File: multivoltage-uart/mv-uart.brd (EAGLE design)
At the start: 37.9 x 33.5 mm, 39 parts, among them SW1 DIP_SP6T, U1 IP4234CZ6, U2 CP2105-GM, U3 LDO_SHD_ADJ-AP2127K-ADJ, X1 MINI-USB-SHIELD-UX60-MB-5ST

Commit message: mv-uart: Add digikey link for all major parts
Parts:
- R1: value 18k -> 18k 1%

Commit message: Complete BOM attributes + export BOM
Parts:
- C3: value 2.2u -> 4.7u

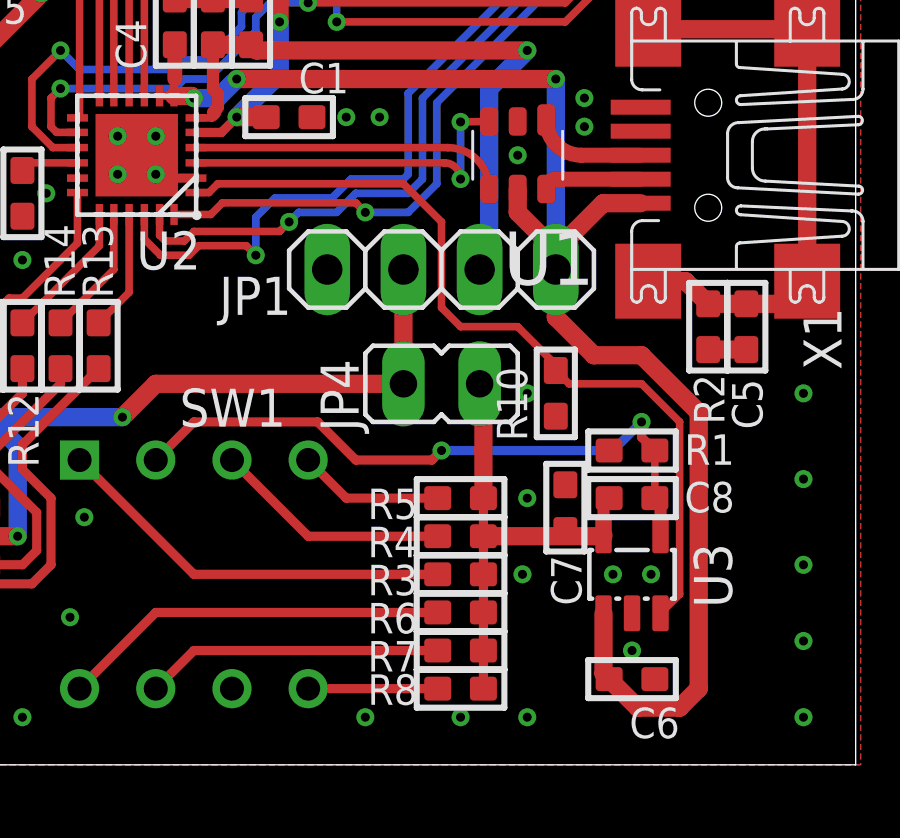
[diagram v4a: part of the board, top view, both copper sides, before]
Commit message: mv-uart: Fix 'board doesn't enumerate if JP4 is closed" issue
Make sure the LDO is always powered up, so the CP2105 internal and
external !RESET pull-ups are towards an active VIO voltage, rather than
one that is switched off by !SUSPEND and thus keeps the CP2105 in reset.

Closes: #1870 (https://osmocom.org/issues/1870)
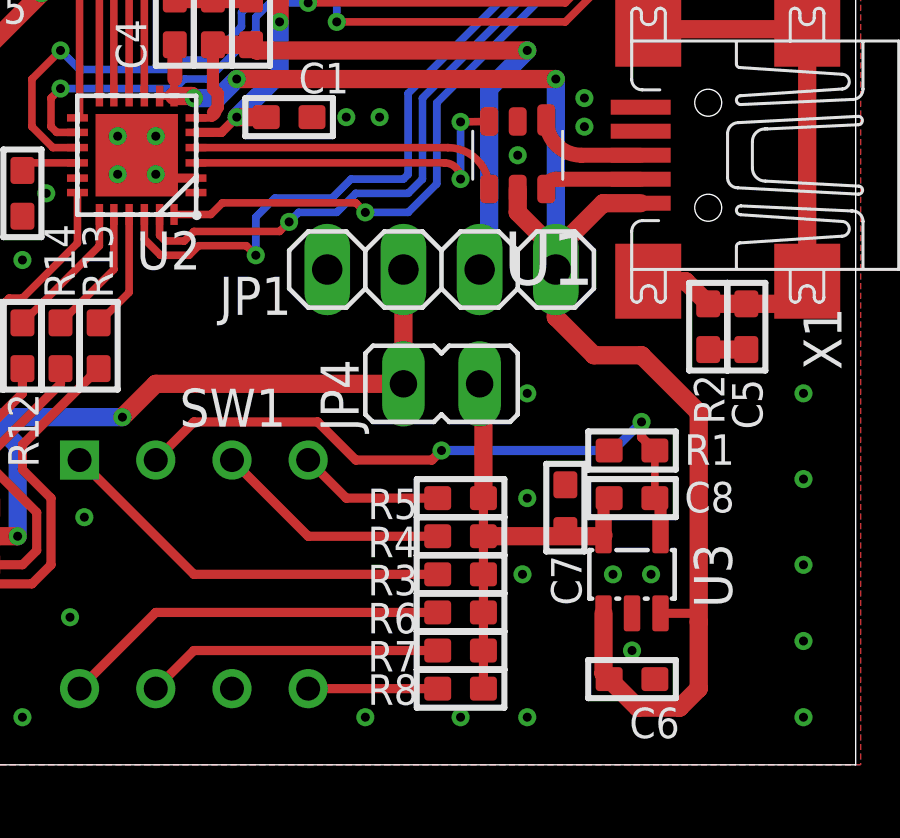
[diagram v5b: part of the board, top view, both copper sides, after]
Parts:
- removed R10: 10k, rc-sysmocom:_0603
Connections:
- net !SUSPEND: no longer R10.2, U3.3
- net GND: no longer R10.1
- net USB_VBUS: now also U3.3
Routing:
- net !SUSPEND: track 28.0 -> 0.00 mm
- net USB_VBUS: track 51.0 -> 52.6 mm
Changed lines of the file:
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@@
 </plain>
 <attributes>
-<attribute name="VERSION" value="v1"/>
+<attribute name="VERSION" value="v2"/>
 </attributes>
 <variantdefs>
@@
 <param name="TopRouterVariant" value="1"/>
 <param name="tpViaShape" value="round"/>
-<param name="PrefDir.1" value="a"/>
+<param name="PrefDir.1" value="|"/>
 <param name="PrefDir.2" value="0"/>
 <param name="PrefDir.3" value="0"/>
@@
 <param name="PrefDir.14" value="0"/>
 <param name="PrefDir.15" value="0"/>
-<param name="PrefDir.16" value="a"/>
+<param name="PrefDir.16" value="-"/>
 <param name="cfVia" value="8"/>
 <param name="cfNonPref" value="5"/>
@@
 <attribute name="LINK" value="http://www.digikey.com/product-detail/en/yageo/RC0603FR-0718KL/311-18.0KHRCT-ND/729936" x="30.48" y="10.4775" size="1.778" layer="27" display="off"/>
 </element>
-<element name="R10" library="rc-sysmocom" package="_0603" value="10k" x="27.94" y="12.3825" smashed="yes" rot="R90">
-<attribute name="NAME" x="26.9875" y="10.795" size="1.016" layer="25" font="vector" ratio="14" rot="R90"/>
-<attribute name="VALUE" x="29.4323" y="10.795" size="0.508" layer="27" font="vector" ratio="10" rot="R90"/>
-<attribute name="DESCRIPTION" value="RES SMD 10K OHM 5% 1/10W 0603" x="27.94" y="12.3825" size="1.778" layer="27" rot="R90" display="off"/>
-<attribute name="MANUFACTURER" value="Samsung Electro-Mechanics America, Inc." x="27.94" y="12.3825" size="1.778" layer="27" rot="R90" display="off"/>
-<attribute name="MANUFACTURERPARTNUMBER" value="RC1608J103CS" x="27.94" y="12.3825" size="1.778" layer="27" rot="R90" display="off"/>
-<attribute name="SOURCE" value="DIGIKEY" x="27.94" y="12.3825" size="1.778" layer="27" rot="R90" display="off"/>
-<attribute name="SOURCEPARTNUMBER" value="1276-5086-1-ND" x="27.94" y="12.3825" size="1.778" layer="27" rot="R90" display="off"/>
-<attribute name="ROHSCERTIFICATE" value="UNKNOWN ROHS CERTIFICATE" x="27.94" y="12.3825" size="1.778" layer="27" rot="R90" display="off"/>
-<attribute name="POPULATED" value="TRUE" x="27.94" y="12.3825" size="1.778" layer="27" rot="R90" display="off"/>
-<attribute name="CLASS" value="RESISTOR" x="27.94" y="12.3825" size="1.778" layer="27" rot="R90" display="off"/>
-<attribute name="LINK" value="http://www.digikey.com/product-detail/en/samsung-electro-mechanics-america-inc/RC1608J103CS/1276-5086-1-ND/3968058" x="27.94" y="12.3825" size="1.778" layer="27" rot="R90" display="off"/>
-</element>
 <element name="R2" library="rc-sysmocom" package="_0603" value="1M" x="33.02" y="14.605" smashed="yes" rot="R90">
 <attribute name="NAME" x="32.54375" y="13.0175" size="1.016" layer="25" font="vector" ratio="14" rot="R270"/>
@@
 <wire x1="29.21" y1="13.6525" x2="30.7975" y2="13.6525" width="0.6096" layer="1"/>
 <wire x1="30.7975" y1="13.6525" x2="32.7025" y2="11.7475" width="0.6096" layer="1"/>
-<wire x1="32.7025" y1="11.7475" x2="32.7025" y2="2.54" width="0.6096" layer="1"/>
+<wire x1="32.7025" y1="11.7475" x2="32.7025" y2="4.7625" width="0.6096" layer="1"/>
+<wire x1="32.7025" y1="4.7625" x2="32.7025" y2="2.54" width="0.6096" layer="1"/>
 <wire x1="32.7025" y1="2.54" x2="32.0675" y2="1.905" width="0.6096" layer="1"/>
 <wire x1="32.0675" y1="1.905" x2="30.6705" y2="1.905" width="0.6096" layer="1"/>
@@
 <wire x1="17.30375" y1="22.86" x2="27.94" y2="22.86" width="0.6096" layer="1"/>
 <via x="27.94" y="22.86" extent="1-16" drill="0.3"/>
+<contactref element="U3" pad="3"/>
+<wire x1="31.43" y1="5.05" x2="32.7025" y2="5.05" width="0.3048" layer="1"/>
+<wire x1="32.7025" y1="5.05" x2="32.7025" y2="4.7625" width="0.3048" layer="1"/>
 </signal>
 <signal name="USB_DN">
@@
 <contactref element="C7" pad="1"/>
 <contactref element="C9" pad="1"/>
-<contactref element="R10" pad="1"/>
 <contactref element="JP2" pad="1"/>
 <contactref element="JP3" pad="1"/>
@@
 </signal>
 <signal name="!SUSPEND">
-<contactref element="U3" pad="3"/>
-<contactref element="R10" pad="2"/>
 <contactref element="U2" pad="1"/>
-<wire x1="15.945" y1="19.0754" x2="16.37665" y2="19.0754" width="0.254" layer="1"/>
-<wire x1="16.37665" y1="19.0754" x2="16.66875" y2="19.3675" width="0.254" layer="1"/>
-<wire x1="16.66875" y1="19.3675" x2="22.86" y2="19.3675" width="0.254" layer="1"/>
-<wire x1="22.86" y1="19.3675" x2="24.13" y2="18.0975" width="0.254" layer="1"/>
-<wire x1="24.13" y1="18.0975" x2="24.13" y2="15.24" width="0.254" layer="1"/>
-<wire x1="24.13" y1="15.24" x2="24.765" y2="14.605" width="0.254" layer="1"/>
-<wire x1="24.765" y1="14.605" x2="26.67" y2="14.605" width="0.254" layer="1"/>
-<wire x1="26.67" y1="14.605" x2="27.94" y2="13.335" width="0.254" layer="1"/>
-<wire x1="27.94" y1="13.335" x2="27.94" y2="13.1445" width="0.254" layer="1"/>
-<wire x1="27.94" y1="13.1445" x2="28.3845" y2="12.7" width="0.254" layer="1"/>
-<wire x1="28.3845" y1="12.7" x2="30.7975" y2="12.7" width="0.254" layer="1"/>
-<wire x1="30.7975" y1="12.7" x2="32.0675" y2="11.43" width="0.254" layer="1"/>
-<wire x1="32.0675" y1="11.43" x2="32.0675" y2="5.6875" width="0.254" layer="1"/>
-<wire x1="32.0675" y1="5.6875" x2="31.43" y2="5.05" width="0.254" layer="1"/>
 </signal>
 <signal name="N$8">
@@
 </signal>
 </signals>
-<errors>
-</errors>
 </board>
 </drawing>
